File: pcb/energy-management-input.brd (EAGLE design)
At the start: 113.3 x 53.7 mm, 72 parts, among them IC4 74HC165N, IC5 74HC165N, J1 WIRE_HOLE-14AWG, J2 WIRE_HOLE-14AWG, J3 WIRE_HOLE-14AWG, J4 WIRE_HOLE-14AWG, U1 DS1307

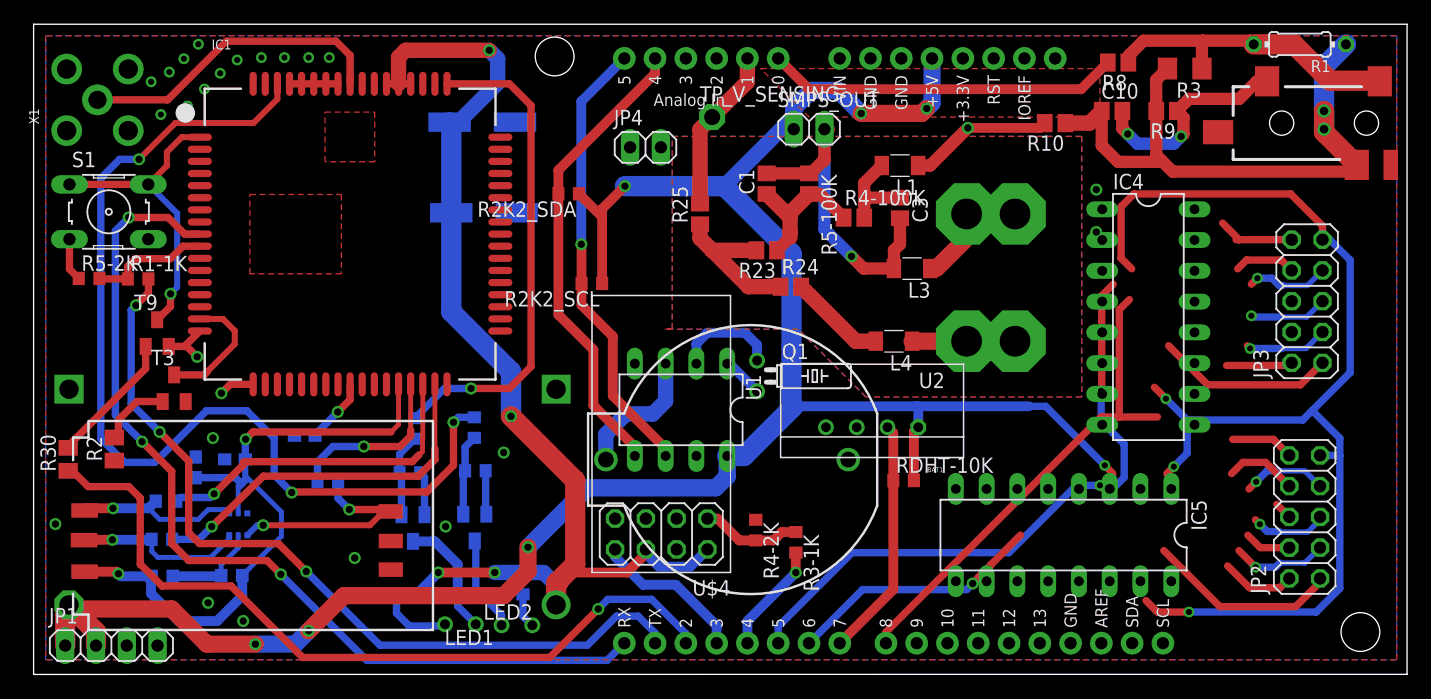
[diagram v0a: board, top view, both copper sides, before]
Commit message: Finished Input Board
Input board schematic and routing finished
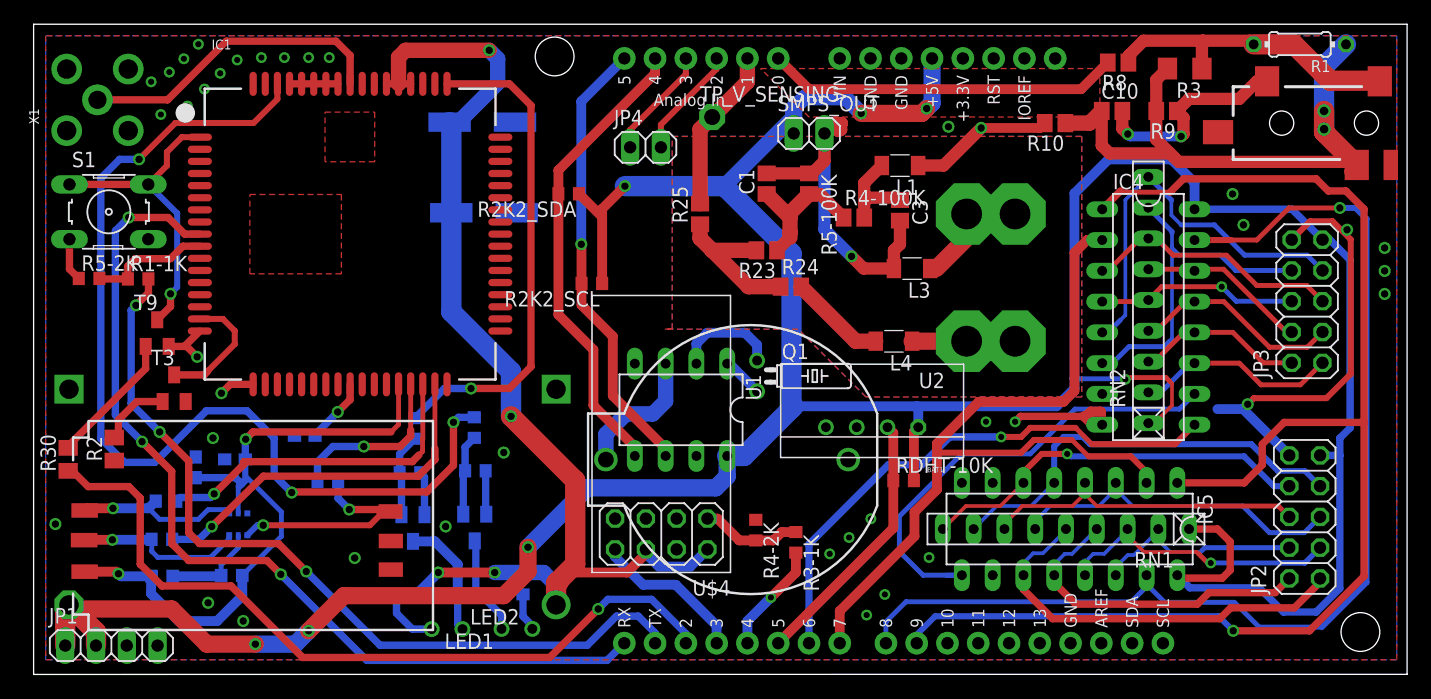
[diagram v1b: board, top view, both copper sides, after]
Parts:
- added RN1, RN2: (no value), resistor-net:RN-9
- moved LED2 1.17 mm to (34.1, 3.74)
- moved IC5 0.71 mm to (85.5, 12.0)
- moved SMPS_OUT 0.35 mm to (64.0, 44.6)
- moved LED1 0.30 mm to (39.9, 3.76)
- moved C3 0.20 mm to (71.5, 38.3)
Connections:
- net CLK: now also U$1.D7; no longer U$1.D9
- net DHT_DATA: now also U$1.D5; no longer U$1.D7
- net OUT_1: now also RN1.5
- net OUT_10: now also RN2.3
- net OUT_11: now also RN2.4
- net OUT_12: now also RN2.6
- net OUT_13: now also RN2.7
- net OUT_14: now also RN2.5
- net OUT_15: now also RN2.9
- net OUT_16: now also RN2.8
- net OUT_2: now also RN1.4
- net OUT_3: now also RN1.3
- net OUT_4: now also RN1.2
- net OUT_5: now also RN1.6
- net OUT_6: now also RN1.7
- net OUT_7: now also RN1.8
- net OUT_8: now also RN1.9
- net OUT_9: now also RN2.2
- net PL: now also U$1.D9; no longer U$1.D5
- net VCC: now also RN1.1, RN2.1
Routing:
- net CLK: track 0.00 -> 66.8 mm
- net PL: track 52.9 -> 113.2 mm, vias 2 -> 1
- net CE: track 40.7 -> 92.2 mm, vias 0 -> 1
- net N$50: track 0.00 -> 38.7 mm
- net GND: track 69.7 -> 107.8 mm, vias 25 -> 39
- net OUT_7: track 7.01 -> 35.2 mm, vias 1 -> 0
- net OUT_8: track 5.95 -> 32.8 mm, vias 0 -> 1
- net OUT_15: track 6.83 -> 33.0 mm, vias 1 -> 0
- net OUT_6: track 1.46 -> 27.6 mm
- net OUT_16: track 5.11 -> 28.9 mm
- net Q7: track 22.6 -> 45.6 mm
- net OUT_5: track 6.41 -> 27.8 mm, vias 1 -> 0
- net OUT_2: track 6.15 -> 27.2 mm
- net OUT_1: track 15.9 -> 33.9 mm
- net OUT_14: track 0.19 -> 16.6 mm, vias 0 -> 1
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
